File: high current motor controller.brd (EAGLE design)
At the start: 100 x 80 mm, 51 parts, among them IC1 LM2676S, Q1 IPT004N03L, Q2 IPT004N03L, Q3 IPT004N03L, Q4 IPT004N03L

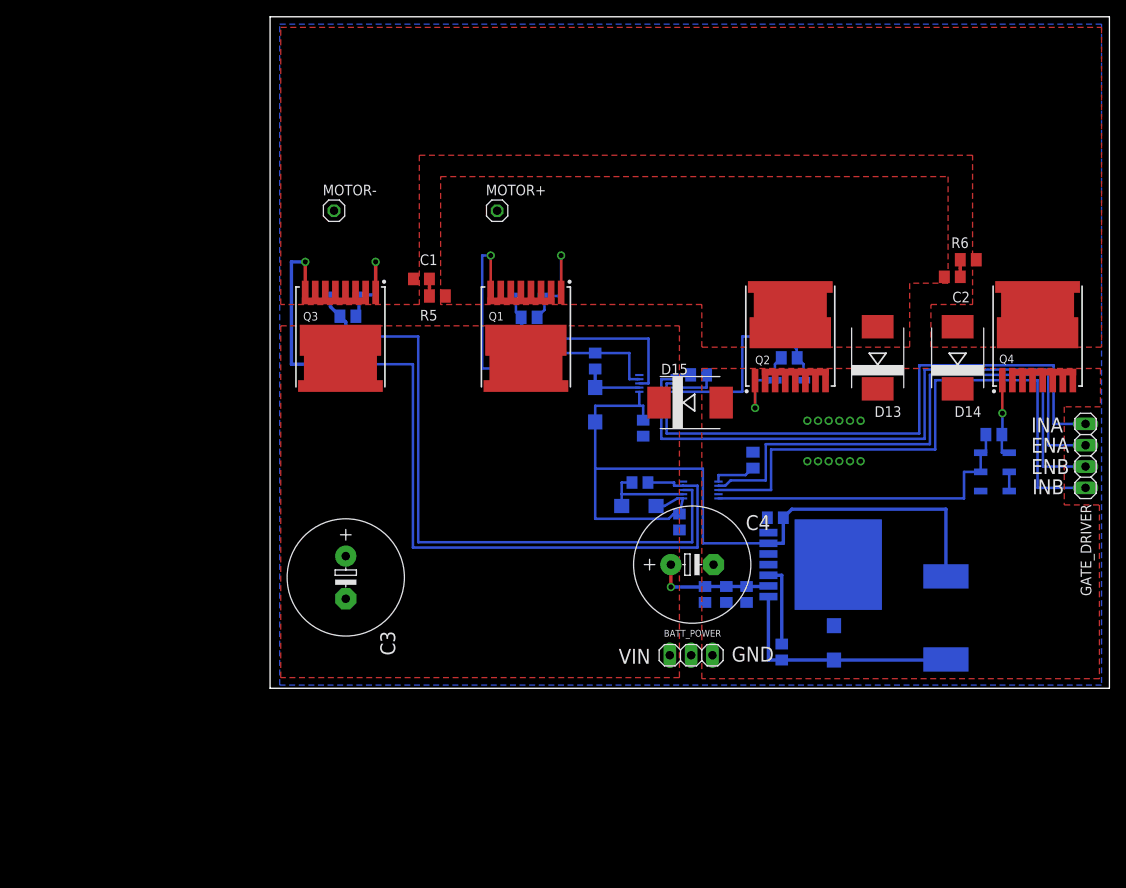
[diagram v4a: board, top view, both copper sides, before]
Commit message: Added library for power and motor connectors; updated schematic with connectors
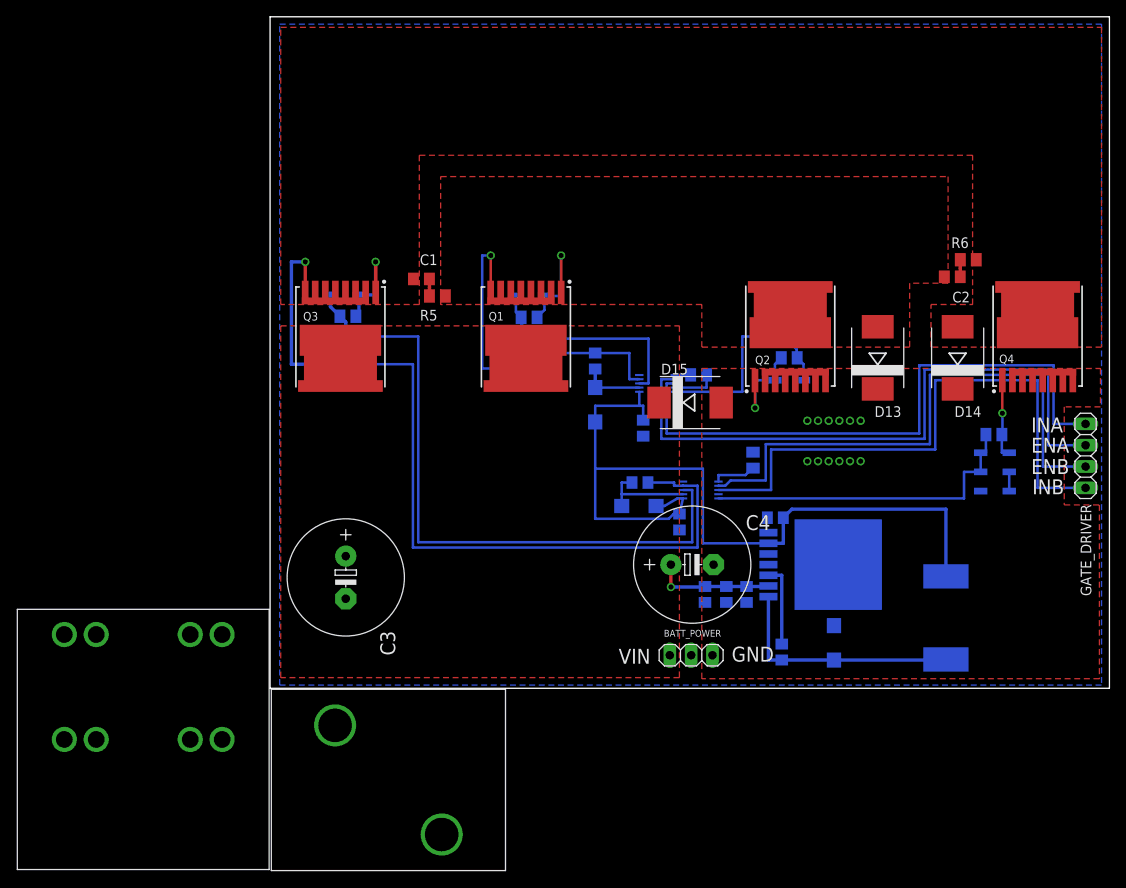
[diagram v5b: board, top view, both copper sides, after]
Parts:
- removed MOTOR+, MOTOR-: (no value), pinhead:1X01
- added U$3: MOLEX_2PIN_50A, connector:MOLEX_50A
- added U$4: TE_2PIN_125A, connector:TE_125A
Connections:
- net AHS: now also U$3.P$1; no longer MOTOR+.1
- net BHS: now also U$3.P$2; no longer MOTOR-.1
- net GND: now also U$4.P$5
- net VIN: now also U$4.P$1
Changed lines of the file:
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@@
 <attribute name="VALUE" x="29.083" y="49.911" size="1.27" layer="28" rot="MR180"/>
 </element>
-<element name="MOTOR+" library="pinhead" package="1X01" value="" x="27.051" y="56.896"/>
-<element name="MOTOR-" library="pinhead" package="1X01" value="" x="7.62" y="56.896"/>
 <element name="Q1" library="IPT004N03L" package="INF-PG-HSOF-8-1-0" value="IPT004N03L" x="30.48" y="41.91" smashed="yes" rot="R270">
 <attribute name="NAME" x="26.035" y="43.815" size="1.016" layer="25"/>
@@
 <attribute name="NAME" x="54.864" y="8.636" size="1.016" layer="26" rot="MR270"/>
 </element>
+<element name="U$3" library="connector" package="MOLEX_50A" value="MOLEX_2PIN_50A" x="14.097" y="-10.922"/>
+<element name="U$4" library="connector" package="TE_125A" value="TE_2PIN_125A" x="-15.113" y="-6.096"/>
 </elements>
 <signals>
@@
 <contactref element="R5" pad="1"/>
 <contactref element="C2" pad="1"/>
-<contactref element="MOTOR+" pad="1"/>
 <contactref element="Q2" pad="9"/>
 <contactref element="D13" pad="A"/>
@@
 <wire x1="32.688" y1="39.243" x2="32.688" y2="39.939" width="0.3048" layer="16"/>
 <wire x1="32.688" y1="39.939" x2="38.735" y2="39.939" width="0.3048" layer="16"/>
+<contactref element="U$3" pad="P$1"/>
+<wire x1="72.39" y1="43.07" x2="80.33" y2="49.022" width="0" layer="19" extent="1-1"/>
+<wire x1="61.976" y1="47.16" x2="72.39" y2="43.07" width="0" layer="19" extent="1-1"/>
+<wire x1="42.799" y1="39.939" x2="61.976" y2="47.16" width="0" layer="19" extent="1-16"/>
+<wire x1="27.48" y1="47.16" x2="26.28" y2="47.16" width="0" layer="19" extent="1-1"/>
+<wire x1="28.68" y1="47.16" x2="27.48" y2="47.16" width="0" layer="19" extent="1-1"/>
+<wire x1="29.88" y1="47.16" x2="28.68" y2="47.16" width="0" layer="19" extent="1-1"/>
+<wire x1="31.08" y1="47.16" x2="29.88" y2="47.16" width="0" layer="19" extent="1-1"/>
+<wire x1="32.28" y1="47.16" x2="31.08" y2="47.16" width="0" layer="19" extent="1-1"/>
+<wire x1="33.48" y1="47.16" x2="32.28" y2="47.16" width="0" layer="19" extent="1-1"/>
+<wire x1="20.889" y1="46.736" x2="26.28" y2="47.16" width="0" layer="19" extent="1-1"/>
+<wire x1="7.747" y1="-4.422" x2="25.273" y2="38.1" width="0" layer="19" extent="16-16"/>
 </signal>
 <signal name="N$6">
@@
 <contactref element="D7" pad="1"/>
 <contactref element="D14" pad="A"/>
-<contactref element="MOTOR-" pad="1"/>
 <contactref element="Q4" pad="9"/>
 <contactref element="Q3" pad="2"/>
@@
 <wire x1="50.927" y1="24.13" x2="49.1949" y2="24.13" width="0.3048" layer="16"/>
 <wire x1="49.1949" y1="24.13" x2="49.1949" y2="24.122" width="0.3048" layer="16"/>
+<contactref element="U$3" pad="P$2"/>
+<wire x1="84.135" y1="51.054" x2="91.44" y2="47.16" width="0" layer="19" extent="1-1"/>
+<wire x1="81.915" y1="43.07" x2="84.135" y2="51.054" width="0" layer="19" extent="1-1"/>
+<wire x1="50.927" y1="24.13" x2="81.915" y2="43.07" width="0" layer="19" extent="1-16"/>
+<wire x1="5.382" y1="47.16" x2="4.182" y2="47.16" width="0" layer="19" extent="1-1"/>
+<wire x1="6.582" y1="47.16" x2="5.382" y2="47.16" width="0" layer="19" extent="1-1"/>
+<wire x1="7.782" y1="47.16" x2="6.582" y2="47.16" width="0" layer="19" extent="1-1"/>
+<wire x1="8.982" y1="47.16" x2="7.782" y2="47.16" width="0" layer="19" extent="1-1"/>
+<wire x1="10.182" y1="47.16" x2="8.982" y2="47.16" width="0" layer="19" extent="1-1"/>
+<wire x1="11.382" y1="47.16" x2="10.182" y2="47.16" width="0" layer="19" extent="1-1"/>
+<wire x1="17.084" y1="48.768" x2="11.382" y2="47.16" width="0" layer="19" extent="1-1"/>
+<wire x1="20.447" y1="-17.422" x2="17.018" y2="16.764" width="0" layer="19" extent="16-16"/>
 </signal>
 <signal name="N$4">
@@
 <contactref element="C9" pad="2"/>
 <contactref element="C10" pad="2"/>
+<contactref element="U$4" pad="P$5"/>
+<wire x1="94.44" y1="36.66" x2="95.64" y2="36.66" width="0" layer="19" extent="1-1"/>
+<wire x1="93.24" y1="36.66" x2="94.44" y2="36.66" width="0" layer="19" extent="1-1"/>
+<wire x1="92.04" y1="36.66" x2="93.24" y2="36.66" width="0" layer="19" extent="1-1"/>
+<wire x1="90.84" y1="36.66" x2="92.04" y2="36.66" width="0" layer="19" extent="1-1"/>
+<wire x1="89.64" y1="36.66" x2="90.84" y2="36.66" width="0" layer="19" extent="1-1"/>
+<wire x1="88.44" y1="36.66" x2="89.64" y2="36.66" width="0" layer="19" extent="1-1"/>
+<wire x1="81.915" y1="35.67" x2="88.44" y2="36.66" width="0" layer="19" extent="1-1"/>
+<wire x1="72.39" y1="35.67" x2="81.915" y2="35.67" width="0" layer="19" extent="1-1"/>
+<wire x1="70.358" y1="31.877" x2="72.39" y2="35.67" width="0" layer="19" extent="1-1"/>
+<wire x1="69.088" y1="31.877" x2="70.358" y2="31.877" width="0" layer="19" extent="1-1"/>
+<wire x1="67.818" y1="31.877" x2="69.088" y2="31.877" width="0" layer="19" extent="1-1"/>
+<wire x1="66.548" y1="31.877" x2="67.818" y2="31.877" width="0" layer="19" extent="1-1"/>
+<wire x1="65.278" y1="31.877" x2="66.548" y2="31.877" width="0" layer="19" extent="1-1"/>
+<wire x1="64.008" y1="31.877" x2="65.278" y2="31.877" width="0" layer="19" extent="1-1"/>
+<wire x1="66.176" y1="36.66" x2="66.548" y2="31.877" width="0" layer="19" extent="1-1"/>
+<wire x1="64.976" y1="36.66" x2="66.176" y2="36.66" width="0" layer="19" extent="1-1"/>
+<wire x1="63.776" y1="36.66" x2="64.976" y2="36.66" width="0" layer="19" extent="1-1"/>
+<wire x1="62.576" y1="36.66" x2="63.776" y2="36.66" width="0" layer="19" extent="1-1"/>
+<wire x1="61.376" y1="36.66" x2="62.576" y2="36.66" width="0" layer="19" extent="1-1"/>
+<wire x1="60.176" y1="36.66" x2="61.376" y2="36.66" width="0" layer="19" extent="1-1"/>
+<wire x1="58.976" y1="36.66" x2="60.176" y2="36.66" width="0" layer="19" extent="1-1"/>
+<wire x1="69.088" y1="27.051" x2="69.088" y2="31.877" width="0" layer="19" extent="1-1"/>
+<wire x1="70.358" y1="27.051" x2="69.088" y2="27.051" width="0" layer="19" extent="1-1"/>
+<wire x1="67.818" y1="27.051" x2="69.088" y2="27.051" width="0" layer="19" extent="1-1"/>
+<wire x1="66.548" y1="27.051" x2="67.818" y2="27.051" width="0" layer="19" extent="1-1"/>
+<wire x1="65.278" y1="27.051" x2="66.548" y2="27.051" width="0" layer="19" extent="1-1"/>
+<wire x1="64.008" y1="27.051" x2="65.278" y2="27.051" width="0" layer="19" extent="1-1"/>
+<wire x1="53.738" y1="34.036" x2="58.976" y2="36.66" width="0" layer="19" extent="1-1"/>
+<wire x1="52.004" y1="35.822" x2="53.738" y2="34.036" width="0" layer="19" extent="1-16"/>
+<wire x1="57.531" y1="28.128" x2="64.008" y2="27.051" width="0" layer="19" extent="16-16"/>
+<wire x1="53.4211" y1="23.122" x2="57.531" y2="28.128" width="0" layer="19" extent="16-16"/>
+<wire x1="48.768" y1="18.862" x2="53.4211" y2="23.122" width="0" layer="19" extent="16-16"/>
+<wire x1="52.832" y1="14.732" x2="48.768" y2="18.862" width="0" layer="19" extent="16-16"/>
+<wire x1="51.816" y1="10.226" x2="52.832" y2="14.732" width="0" layer="19" extent="16-16"/>
+<wire x1="54.356" y1="10.226" x2="51.816" y2="10.226" width="0" layer="19" extent="16-16"/>
+<wire x1="56.769" y1="10.226" x2="54.356" y2="10.226" width="0" layer="19" extent="16-16"/>
+<wire x1="59.371" y1="14.732" x2="56.769" y2="10.226" width="0" layer="19" extent="16-16"/>
+<wire x1="59.248" y1="20.32" x2="59.371" y2="14.732" width="0" layer="19" extent="16-16"/>
+<wire x1="52.705" y1="3.937" x2="51.816" y2="10.226" width="0" layer="19" extent="16-16"/>
+<wire x1="44.45" y1="30.038" x2="48.2141" y2="35.822" width="0" layer="19" extent="16-16"/>
+<wire x1="59.895" y1="44.196" x2="60.176" y2="36.66" width="0" layer="19" extent="1-16"/>
+<wire x1="67.182" y1="7.462" x2="59.371" y2="14.732" width="0" layer="19" extent="16-16"/>
+<wire x1="84.66" y1="23.495" x2="81.915" y2="35.67" width="0" layer="19" extent="1-16"/>
+<wire x1="9.017" y1="10.668" x2="44.45" y2="30.038" width="0" layer="19" extent="16-16"/>
+<wire x1="-9.513" y1="6.404" x2="9.017" y2="10.668" width="0" layer="19" extent="1-1"/>
 </signal>
 <signal name="12V">
@@
 <via x="47.752" y="12.065" extent="1-16" drill="0.6"/>
 <wire x1="47.752" y1="12.065" x2="47.752" y2="14.732" width="0.4064" layer="1"/>
+<contactref element="U$4" pad="P$1"/>
+<wire x1="30.48" y1="36.66" x2="46.338" y2="34.036" width="0" layer="19" extent="1-1"/>
+<wire x1="47.752" y1="14.732" x2="46.338" y2="34.036" width="0" layer="19" extent="1-1"/>
+<wire x1="47.625" y1="3.937" x2="47.752" y2="12.065" width="0" layer="19" extent="16-16"/>
+<wire x1="8.382" y1="36.66" x2="30.48" y2="36.66" width="0" layer="19" extent="1-1"/>
+<wire x1="9.017" y1="15.748" x2="8.382" y2="36.66" width="0" layer="19" extent="1-1"/>
+<wire x1="-24.513" y1="6.404" x2="9.017" y2="15.748" width="0" layer="19" extent="1-1"/>
 </signal>
 <signal name="N$16">

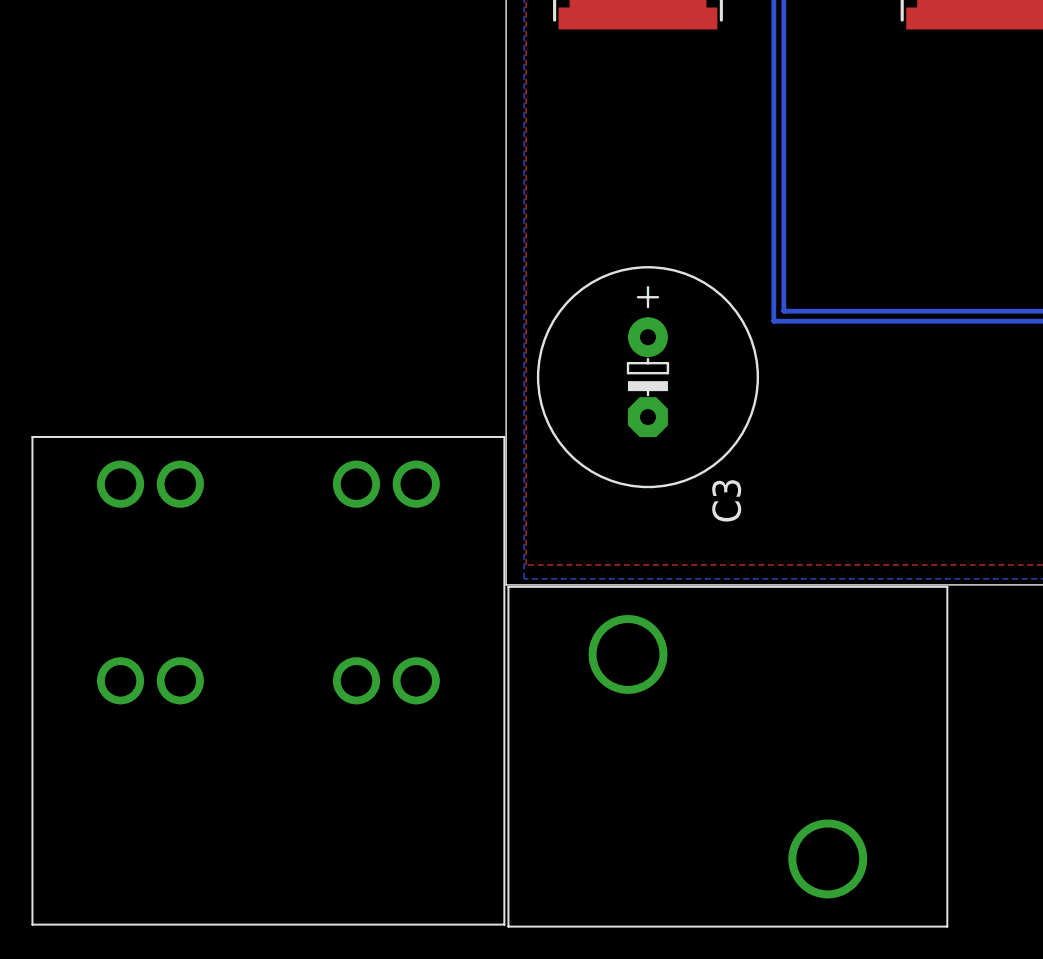
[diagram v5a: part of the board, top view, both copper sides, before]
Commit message: Updated connector library to use all pads of power connector
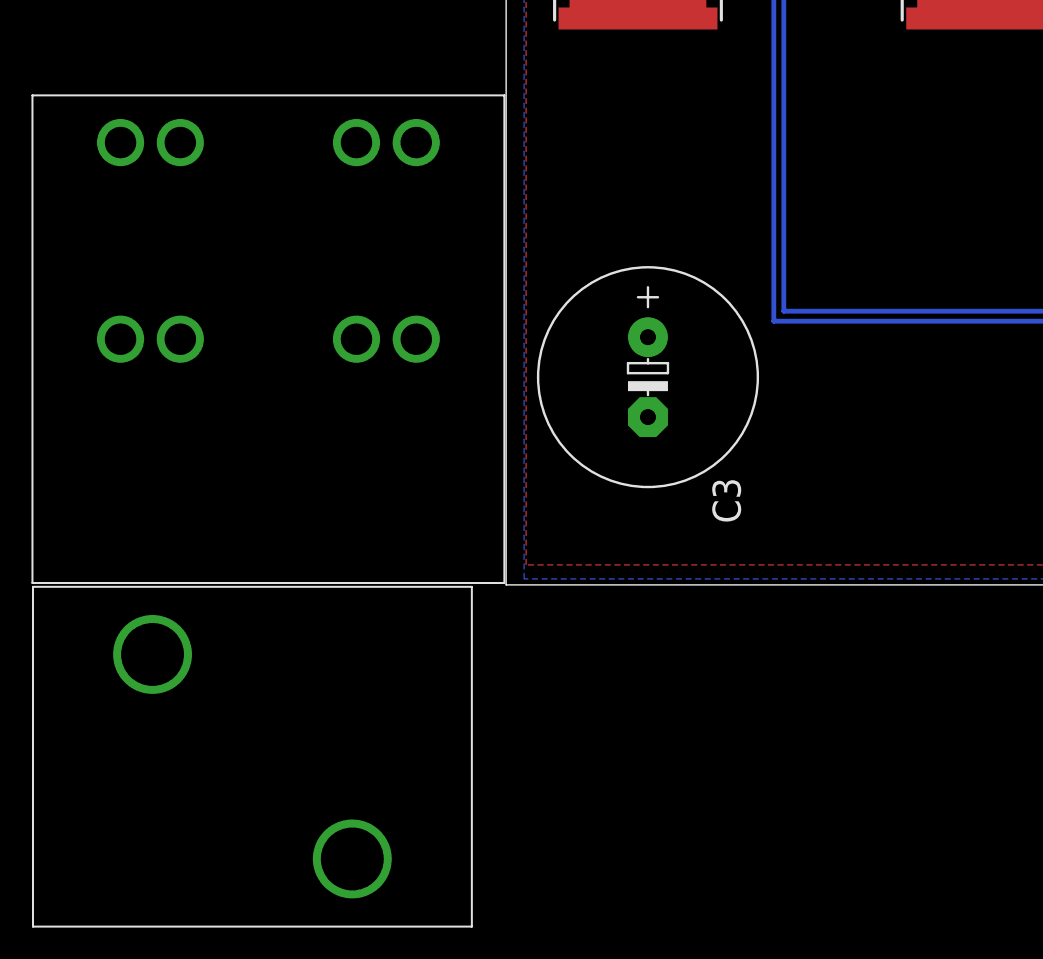
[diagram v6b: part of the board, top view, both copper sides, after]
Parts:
- U$3: value MOLEX_2PIN_50A -> TE_2PIN_125A; device connector:MOLEX_50A -> connector:TE_125A
- U$4: value TE_2PIN_125A -> MOLEX_2PIN_50A; device connector:TE_125A -> connector:MOLEX_50A
- moved U$3 39.5 mm to (-15.1, 15.6)
- moved U$4 4.93 mm to (-16.1, -10.9)
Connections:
- net AHS: now also U$4.P$1; no longer U$3.P$1
- net BHS: now also U$4.P$2; no longer U$3.P$2
- net GND: now also U$3.P$5, U$3.P$6, U$3.P$7, U$3.P$8; no longer U$4.P$5
- net VIN: now also U$3.P$1, U$3.P$1.1, U$3.P$1.2, U$3.P$1.3; no longer U$4.P$1
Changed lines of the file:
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@@
 <attribute name="NAME" x="54.864" y="8.636" size="1.016" layer="26" rot="MR270"/>
 </element>
-<element name="U$3" library="connector" package="MOLEX_50A" value="MOLEX_2PIN_50A" x="14.097" y="-10.922"/>
-<element name="U$4" library="connector" package="TE_125A" value="TE_2PIN_125A" x="-15.113" y="-6.096"/>
+<element name="U$3" library="connector" package="TE_125A" value="TE_2PIN_125A" x="-15.113" y="15.621"/>
+<element name="U$4" library="connector" package="MOLEX_50A" value="MOLEX_2PIN_50A" x="-16.129" y="-10.922"/>
 </elements>
 <signals>
@@
 <wire x1="32.688" y1="39.243" x2="32.688" y2="39.939" width="0.3048" layer="16"/>
 <wire x1="32.688" y1="39.939" x2="38.735" y2="39.939" width="0.3048" layer="16"/>
-<contactref element="U$3" pad="P$1"/>
+<contactref element="U$4" pad="P$1"/>
 <wire x1="72.39" y1="43.07" x2="80.33" y2="49.022" width="0" layer="19" extent="1-1"/>
 <wire x1="61.976" y1="47.16" x2="72.39" y2="43.07" width="0" layer="19" extent="1-1"/>
@@
 <wire x1="33.48" y1="47.16" x2="32.28" y2="47.16" width="0" layer="19" extent="1-1"/>
 <wire x1="20.889" y1="46.736" x2="26.28" y2="47.16" width="0" layer="19" extent="1-1"/>
-<wire x1="7.747" y1="-4.422" x2="25.273" y2="38.1" width="0" layer="19" extent="16-16"/>
+<wire x1="-22.479" y1="-4.422" x2="25.273" y2="38.1" width="0" layer="19" extent="16-16"/>
 </signal>
 <signal name="N$6">
@@
 <wire x1="50.927" y1="24.13" x2="49.1949" y2="24.13" width="0.3048" layer="16"/>
 <wire x1="49.1949" y1="24.13" x2="49.1949" y2="24.122" width="0.3048" layer="16"/>
-<contactref element="U$3" pad="P$2"/>
+<contactref element="U$4" pad="P$2"/>
 <wire x1="84.135" y1="51.054" x2="91.44" y2="47.16" width="0" layer="19" extent="1-1"/>
 <wire x1="81.915" y1="43.07" x2="84.135" y2="51.054" width="0" layer="19" extent="1-1"/>
@@
 <wire x1="11.382" y1="47.16" x2="10.182" y2="47.16" width="0" layer="19" extent="1-1"/>
 <wire x1="17.084" y1="48.768" x2="11.382" y2="47.16" width="0" layer="19" extent="1-1"/>
-<wire x1="20.447" y1="-17.422" x2="17.018" y2="16.764" width="0" layer="19" extent="16-16"/>
+<wire x1="-9.779" y1="-17.422" x2="17.018" y2="16.764" width="0" layer="19" extent="16-16"/>
 </signal>
 <signal name="N$4">
@@
 <contactref element="C9" pad="2"/>
 <contactref element="C10" pad="2"/>
-<contactref element="U$4" pad="P$5"/>
+<contactref element="U$3" pad="P$6"/>
+<contactref element="U$3" pad="P$8"/>
+<contactref element="U$3" pad="P$5"/>
+<contactref element="U$3" pad="P$7"/>
 <wire x1="94.44" y1="36.66" x2="95.64" y2="36.66" width="0" layer="19" extent="1-1"/>
 <wire x1="93.24" y1="36.66" x2="94.44" y2="36.66" width="0" layer="19" extent="1-1"/>
@@
 <wire x1="84.66" y1="23.495" x2="81.915" y2="35.67" width="0" layer="19" extent="1-16"/>
 <wire x1="9.017" y1="10.668" x2="44.45" y2="30.038" width="0" layer="19" extent="16-16"/>
-<wire x1="-9.513" y1="6.404" x2="9.017" y2="10.668" width="0" layer="19" extent="1-1"/>
+<wire x1="-5.713" y1="15.621" x2="9.017" y2="10.668" width="0" layer="19" extent="1-1"/>
+<wire x1="-9.513" y1="15.621" x2="-5.713" y2="15.621" width="0" layer="19" extent="1-1"/>
+<wire x1="-5.713" y1="28.121" x2="-5.713" y2="15.621" width="0" layer="19" extent="1-1"/>
+<wire x1="-9.513" y1="28.121" x2="-5.713" y2="28.121" width="0" layer="19" extent="1-1"/>
 </signal>
 <signal name="12V">
@@
 <via x="47.752" y="12.065" extent="1-16" drill="0.6"/>
 <wire x1="47.752" y1="12.065" x2="47.752" y2="14.732" width="0.4064" layer="1"/>
-<contactref element="U$4" pad="P$1"/>
+<contactref element="U$3" pad="P$1.2"/>
+<contactref element="U$3" pad="P$1"/>
+<contactref element="U$3" pad="P$1.3"/>
+<contactref element="U$3" pad="P$1.1"/>
 <wire x1="30.48" y1="36.66" x2="46.338" y2="34.036" width="0" layer="19" extent="1-1"/>
 <wire x1="47.752" y1="14.732" x2="46.338" y2="34.036" width="0" layer="19" extent="1-1"/>
@@
 <wire x1="8.382" y1="36.66" x2="30.48" y2="36.66" width="0" layer="19" extent="1-1"/>
 <wire x1="9.017" y1="15.748" x2="8.382" y2="36.66" width="0" layer="19" extent="1-1"/>
-<wire x1="-24.513" y1="6.404" x2="9.017" y2="15.748" width="0" layer="19" extent="1-1"/>
+<wire x1="-20.713" y1="15.621" x2="9.017" y2="15.748" width="0" layer="19" extent="1-1"/>
+<wire x1="-24.513" y1="15.621" x2="-20.713" y2="15.621" width="0" layer="19" extent="1-1"/>
+<wire x1="-20.713" y1="28.121" x2="-20.713" y2="15.621" width="0" layer="19" extent="1-1"/>
+<wire x1="-24.513" y1="28.121" x2="-20.713" y2="28.121" width="0" layer="19" extent="1-1"/>
 </signal>
 <signal name="N$16">
